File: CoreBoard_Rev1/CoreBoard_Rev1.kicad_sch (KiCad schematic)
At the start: 84 parts, among them J1 RJ45_LED_Shielded, SW1 SW_Push, SW10 SW_Push, SW11 SW_Push, SW12 SW_Push, SW13 SW_Push, SW14 SW_Push, SW15 SW_Push, SW16 SW_SPDT, SW2 SW_Push, SW3 SW_Push, SW4 SW_Push, SW5 SW_Push, SW6 SW_Push, SW7 SW_Push, SW8 SW_Push, SW9 SW_Push, U1 Teensy4.1_DEV-16771, U2 TSR_1-2450, U3 TSR_1-2450, U4 74HC148, U5 74HC148, U6 74HC00

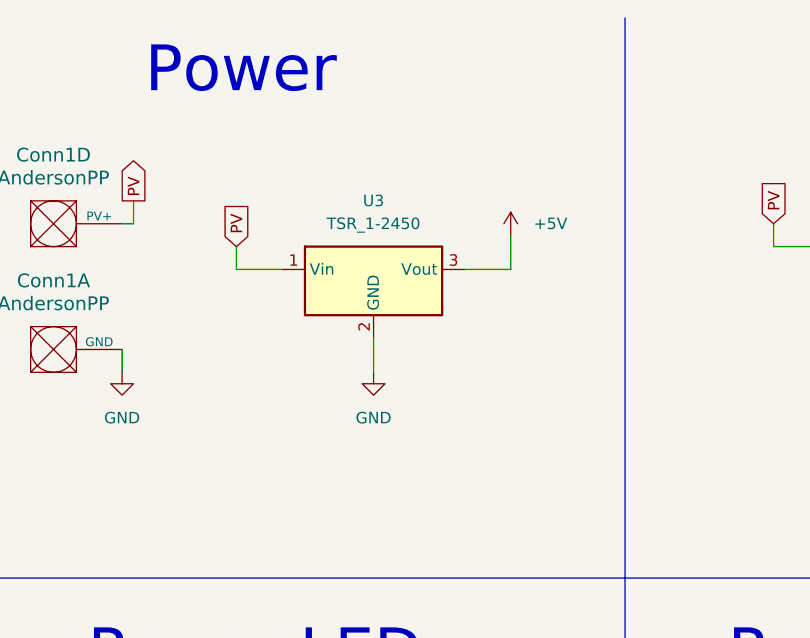
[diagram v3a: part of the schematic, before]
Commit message: Changes to OKI, BOM Regeneration
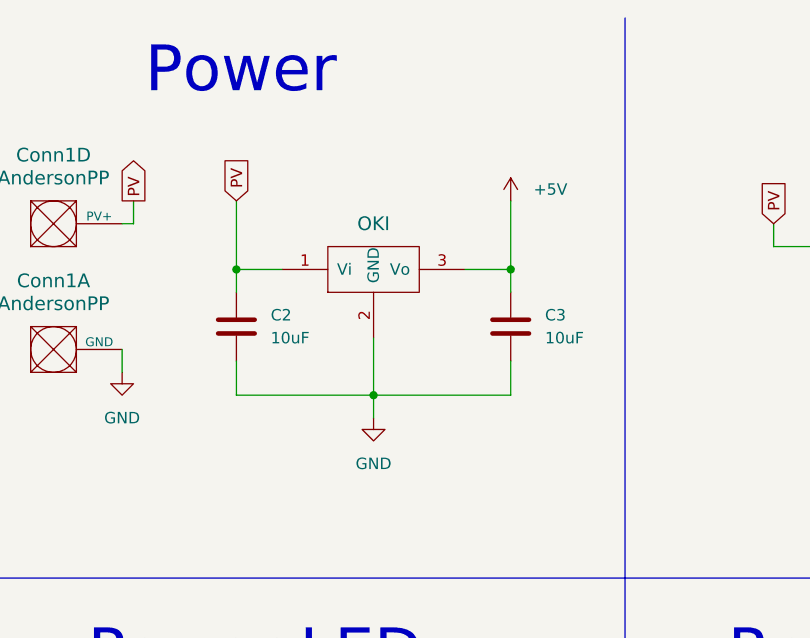
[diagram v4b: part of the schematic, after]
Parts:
- removed U3: TSR_1-2450, Converter_DCDC:Converter_DCDC_TRACO_TSR-1_THT, symbol Regulator_Switching:TSR_1-2450
- added C2, C3: 10uF, Capacitor_SMD:C_0603_1608Metric_Pad1.08x0.95mm_HandSolder, symbol Device:C
- added U7: OKI, MRDT_Devices:OKI_Horizontal, symbol MRDT_Devices:OKI
- U6: footprint (none) -> Package_SO:SO-14_5.3x10.2mm_P1.27mm
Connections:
- net +5V: now also C3.1, U7.3 (Vo)
- net GND: now also C2.2, C3.2, U7.2 (GND)
- net PV: now also C2.1, U7.1 (Vi)
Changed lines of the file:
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@@
   (junction (at 224.79 251.46) (diameter 0) (color 0 0 0 0)
   )
+  (junction (at 63.5 54.61) (diameter 0) (color 0 0 0 0)
+  )
   (junction (at 308.61 53.34) (diameter 0) (color 0 0 0 0)
   )
@@
   (junction (at 189.23 147.32) (diameter 0) (color 0 0 0 0)
   )
+  (junction (at 78.74 40.64) (diameter 0) (color 0 0 0 0)
+  )
   (junction (at 247.65 119.38) (diameter 0) (color 0 0 0 0)
   )
@@
   (junction (at 369.57 48.26) (diameter 0) (color 0 0 0 0)
   )
+  (junction (at 48.26 40.64) (diameter 0) (color 0 0 0 0)
+  )
   (junction (at 212.09 259.08) (diameter 0) (color 0 0 0 0)
   )
@@
     (stroke (width 0) (type default))
   )
+  (wire (pts (xy 63.5 54.61) (xy 63.5 57.15))
+    (stroke (width 0) (type default))
+  )
   (wire (pts (xy 337.82 53.34) (xy 344.17 53.34))
     (stroke (width 0) (type default))
@@
     (stroke (width 0) (type default))
   )
+  (wire (pts (xy 78.74 40.64) (xy 78.74 43.18))
+    (stroke (width 0) (type default))
+  )
   (wire (pts (xy 337.82 53.34) (xy 337.82 63.5))
     (stroke (width 0) (type default))
@@
     (stroke (width 0) (type default))
   )
-  (wire (pts (xy 63.5 48.26) (xy 63.5 52.07))
-    (stroke (width 0) (type default))
-  )
   (wire (pts (xy 363.22 139.7) (xy 363.22 214.63))
     (stroke (width 0) (type default))
@@
     (stroke (width 0) (type default))
   )
-  (wire (pts (xy 78.74 40.64) (xy 78.74 36.83))
+  (wire (pts (xy 78.74 40.64) (xy 78.74 33.02))
     (stroke (width 0) (type default))
   )
@@
     (stroke (width 0) (type default))
   )
+  (wire (pts (xy 48.26 50.8) (xy 48.26 54.61))
+    (stroke (width 0) (type default))
+  )
   (wire (pts (xy 260.35 130.81) (xy 260.35 128.27))
     (stroke (width 0) (type default))
@@
     (stroke (width 0) (type default))
   )
+  (wire (pts (xy 48.26 40.64) (xy 48.26 43.18))
+    (stroke (width 0) (type default))
+  )
   (polyline (pts (xy 91.44 12.7) (xy 91.44 74.93))
     (stroke (width 0) (type default))
@@
     (stroke (width 0) (type default))
   )
+  (wire (pts (xy 78.74 50.8) (xy 78.74 54.61))
+    (stroke (width 0) (type default))
+  )
   (wire (pts (xy 50.8 185.42) (xy 50.8 180.34))
     (stroke (width 0) (type default))
@@
     (stroke (width 0) (type default))
   )
+  (wire (pts (xy 63.5 48.26) (xy 63.5 54.61))
+    (stroke (width 0) (type default))
+  )
   (wire (pts (xy 275.59 189.23) (xy 283.21 189.23))
     (stroke (width 0) (type default))
@@
     (stroke (width 0) (type default))
   )
+  (wire (pts (xy 48.26 54.61) (xy 63.5 54.61))
+    (stroke (width 0) (type default))
+  )
   (wire (pts (xy 281.94 147.32) (xy 283.21 147.32))
     (stroke (width 0) (type default))
@@
     (stroke (width 0) (type default))
   )
-  (wire (pts (xy 48.26 38.1) (xy 48.26 40.64))
+  (wire (pts (xy 48.26 33.02) (xy 48.26 40.64))
     (stroke (width 0) (type default))
   )
@@
     (stroke (width 0) (type default))
   )
+  (wire (pts (xy 78.74 54.61) (xy 63.5 54.61))
+    (stroke (width 0) (type default))
+  )
   (wire (pts (xy 358.14 222.25) (xy 337.82 222.25))
     (stroke (width 0) (type default))
@@
     )
   )
-  (global_label "PV" (shape input) (at 48.26 38.1 90) (fields_autoplaced)
+  (global_label "PV" (shape input) (at 48.26 33.02 90) (fields_autoplaced)
     (effects (font (size 1.27 1.27)) (justify left))
-    (property "Intersheetrefs" "${INTERSHEET_REFS}" (at 48.26 32.7562 90)
+    (property "Intersheetrefs" "${INTERSHEET_REFS}" (at 48.26 27.6762 90)
       (effects (font (size 1.27 1.27)) (justify left) hide)
     )
@@
     )
   )
-  (symbol (lib_id "power:+5V") (at 78.74 36.83 0) (unit 1)
+  (symbol (lib_id "power:+5V") (at 78.74 33.02 0) (unit 1)
     (in_bom yes) (on_board yes) (dnp no) (fields_autoplaced)
-    (property "Reference" "#PWR012" (at 78.74 40.64 0)
+    (property "Reference" "#PWR012" (at 78.74 36.83 0)
       (effects (font (size 1.27 1.27)) hide)
     )
-    (property "Value" "+5V" (at 81.28 35.56 0)
+    (property "Value" "+5V" (at 81.28 31.75 0)
       (effects (font (size 1.27 1.27)) (justify left))
     )
-    (property "Footprint" "" (at 78.74 36.83 0)
+    (property "Footprint" "" (at 78.74 33.02 0)
       (effects (font (size 1.27 1.27)) hide)
     )
-    (property "Datasheet" "" (at 78.74 36.83 0)
+    (property "Datasheet" "" (at 78.74 33.02 0)
       (effects (font (size 1.27 1.27)) hide)
     )
@@
     )
   )
+  (symbol (lib_id "MRDT_Devices:OKI") (at 58.42 43.18 0) (unit 1)
+    (in_bom yes) (on_board yes) (dnp no) (fields_autoplaced)
+    (property "Reference" "U7" (at 59.69 44.45 0)
+      (effects (font (size 1.524 1.524)) hide)
+    )
+    (property "Value" "OKI" (at 63.5 35.56 0)
+      (effects (font (size 1.524 1.524)))
+    )
+    (property "Footprint" "MRDT_Devices:OKI_Horizontal" (at 53.34 45.72 0)
+      (effects (font (size 1.524 1.524)) hide)
+    )
+    (property "Datasheet" "" (at 53.34 45.72 0)
+      (effects (font (size 1.524 1.524)) hide)
+    )
+    (pin "1")
+    (pin "2")
+    (pin "3")
+    (instances
+      (project "CoreBoard_Rev1"
+        (path "/33647808-cf2c-4b1c-bf2f-58fa6408b099"
+          (reference "U7") (unit 1)
+        )
+      )
+    )
+  )
   (symbol (lib_id "power:GND") (at 337.82 66.04 0) (unit 1)
     (in_bom yes) (on_board yes) (dnp no) (fields_autoplaced)
@@
       (effects (font (size 1.27 1.27)) (justify left))
     )
-    (property "Footprint" "" (at 384.81 121.92 0)
+    (property "Footprint" "Package_SO:SO-14_5.3x10.2mm_P1.27mm" (at 384.81 121.92 0)
       (effects (font (size 1.27 1.27)) hide)
     )
@@
       (effects (font (size 1.27 1.27)))
     )
-    (property "Footprint" "" (at 382.27 217.17 0)
+    (property "Footprint" "Package_SO:SO-14_5.3x10.2mm_P1.27mm" (at 382.27 217.17 0)
       (effects (font (size 1.27 1.27)) hide)
     )
@@
     )
   )
-  (symbol (lib_id "power:GND") (at 63.5 52.07 0) (unit 1)
+  (symbol (lib_id "power:GND") (at 63.5 57.15 0) (unit 1)
     (in_bom yes) (on_board yes) (dnp no) (fields_autoplaced)
-    (property "Reference" "#PWR013" (at 63.5 58.42 0)
+    (property "Reference" "#PWR013" (at 63.5 63.5 0)
       (effects (font (size 1.27 1.27)) hide)
     )
-    (property "Value" "GND" (at 63.5 57.15 0)
+    (property "Value" "GND" (at 63.5 62.23 0)
       (effects (font (size 1.27 1.27)))
     )
-    (property "Footprint" "" (at 63.5 52.07 0)
+    (property "Footprint" "" (at 63.5 57.15 0)
       (effects (font (size 1.27 1.27)) hide)
     )
-    (property "Datasheet" "" (at 63.5 52.07 0)
+    (property "Datasheet" "" (at 63.5 57.15 0)
       (effects (font (size 1.27 1.27)) hide)
     )
@@
     )
   )
+  (symbol (lib_id "Device:C") (at 48.26 46.99 0) (unit 1)
+    (in_bom yes) (on_board yes) (dnp no) (fields_autoplaced)
+    (property "Reference" "C2" (at 52.07 45.72 0)
+      (effects (font (size 1.27 1.27)) (justify left))
+    )
+    (property "Value" "10uF" (at 52.07 48.26 0)
+      (effects (font (size 1.27 1.27)) (justify left))
+    )
+    (property "Footprint" "Capacitor_SMD:C_0603_1608Metric_Pad1.08x0.95mm_HandSolder" (at 49.2252 50.8 0)
+      (effects (font (size 1.27 1.27)) hide)
+    )
+    (property "Datasheet" "~" (at 48.26 46.99 0)
+      (effects (font (size 1.27 1.27)) hide)
+    )
+    (pin "1")
+    (pin "2")
+    (instances
+      (project "CoreBoard_Rev1"
+        (path "/33647808-cf2c-4b1c-bf2f-58fa6408b099"
+          (reference "C2") (unit 1)
+        )
+      )
+    )
+  )
   (symbol (lib_id "power:GND") (at 99.06 273.05 0) (unit 1)
     (in_bom yes) (on_board yes) (dnp no) (fields_autoplaced)
@@
       (effects (font (size 1.27 1.27)))
     )
-    (property "Footprint" "" (at 382.27 181.61 0)
+    (property "Footprint" "Package_SO:SO-14_5.3x10.2mm_P1.27mm" (at 382.27 181.61 0)
       (effects (font (size 1.27 1.27)) hide)
     )
@@
       (effects (font (size 1.27 1.27)))
     )
-    (property "Footprint" "" (at 382.27 199.39 0)
+    (property "Footprint" "Package_SO:SO-14_5.3x10.2mm_P1.27mm" (at 382.27 199.39 0)
       (effects (font (size 1.27 1.27)) hide)
     )
@@
     )
   )
-  (symbol (lib_id "Regulator_Switching:TSR_1-2450") (at 63.5 43.18 0) (unit 1)
-    (in_bom yes) (on_board yes) (dnp no) (fields_autoplaced)
-    (property "Reference" "U3" (at 63.5 33.02 0)
-      (effects (font (size 1.27 1.27)))
-    )
-    (property "Value" "TSR_1-2450" (at 63.5 35.56 0)
-      (effects (font (size 1.27 1.27)))
-    )
-    (property "Footprint" "Converter_DCDC:Converter_DCDC_TRACO_TSR-1_THT" (at 63.5 46.99 0)
-      (effects (font (size 1.27 1.27) italic) (justify left) hide)
-    )
-    (property "Datasheet" "http://www.tracopower.com/products/tsr1.pdf" (at 63.5 43.18 0)
-      (effects (font (size 1.27 1.27)) hide)
-    )
-    (pin "1")
-    (pin "2")
-    (pin "3")
-    (instances
-      (project "CoreBoard_Rev1"
-        (path "/33647808-cf2c-4b1c-bf2f-58fa6408b099"
-          (reference "U3") (unit 1)
-        )
-      )
-    )
-  )
   (symbol (lib_id "Switch:SW_Push") (at 271.78 198.12 0) (unit 1)
     (in_bom yes) (on_board yes) (dnp no)
@@
         )
       )
+    )
+  )
+  (symbol (lib_id "Device:C") (at 78.74 46.99 0) (unit 1)
+    (in_bom yes) (on_board yes) (dnp no) (fields_autoplaced)
+    (property "Reference" "C3" (at 82.55 45.72 0)
+      (effects (font (size 1.27 1.27)) (justify left))
+    )
+    (property "Value" "10uF" (at 82.55 48.26 0)
+      (effects (font (size 1.27 1.27)) (justify left))
+    )
+    (property "Footprint" "Capacitor_SMD:C_0603_1608Metric_Pad1.08x0.95mm_HandSolder" (at 79.7052 50.8 0)
+      (effects (font (size 1.27 1.27)) hide)
+    )
+    (property "Datasheet" "~" (at 78.74 46.99 0)
+      (effects (font (size 1.27 1.27)) hide)
+    )
+    (pin "1")
+    (pin "2")
+    (instances
+      (project "CoreBoard_Rev1"
+        (path "/33647808-cf2c-4b1c-bf2f-58fa6408b099"
+          (reference "C3") (unit 1)
+        )
+      )

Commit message: completed rev1 rough draft
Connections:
- net RL_TX is gone; now on net BR_RX: U1.14 (A0)
- net BL_RX: now also U1.29 (TX7); no longer U1.15 (A1)
- net BL_TX: now also U1.28 (RX7); no longer Conn3.9
- net BR_RX: no longer U1.28 (RX7)
- net BR_TX: now also Conn3.9, U1.15 (A1); no longer U1.29 (TX7)
- net FL_TX: no longer Conn3.3
- net FR_TX: now also Conn3.3
- net ServoPWM5: no longer Conn5.3, U1.9 (OUT1C)
- net ServoPWM7: now also Conn6.9; no longer Conn6.3
- net ServoPWM9: now also Conn6.3; no longer Conn6.9
- new net ServoPWM6: Conn5.3, U1.9 (OUT1C)
